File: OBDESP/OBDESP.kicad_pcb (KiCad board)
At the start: 2 copper layers, 56.8 x 26 mm, 38 parts, among them J1 USB_A, J2 RST, J3 BOOT, J4 UART, Q1 BC848CLT1G, U1 NCP1117-3.3_DPAK, U2 ESP32-WROOM-32, U3 NRF24L01_SMD

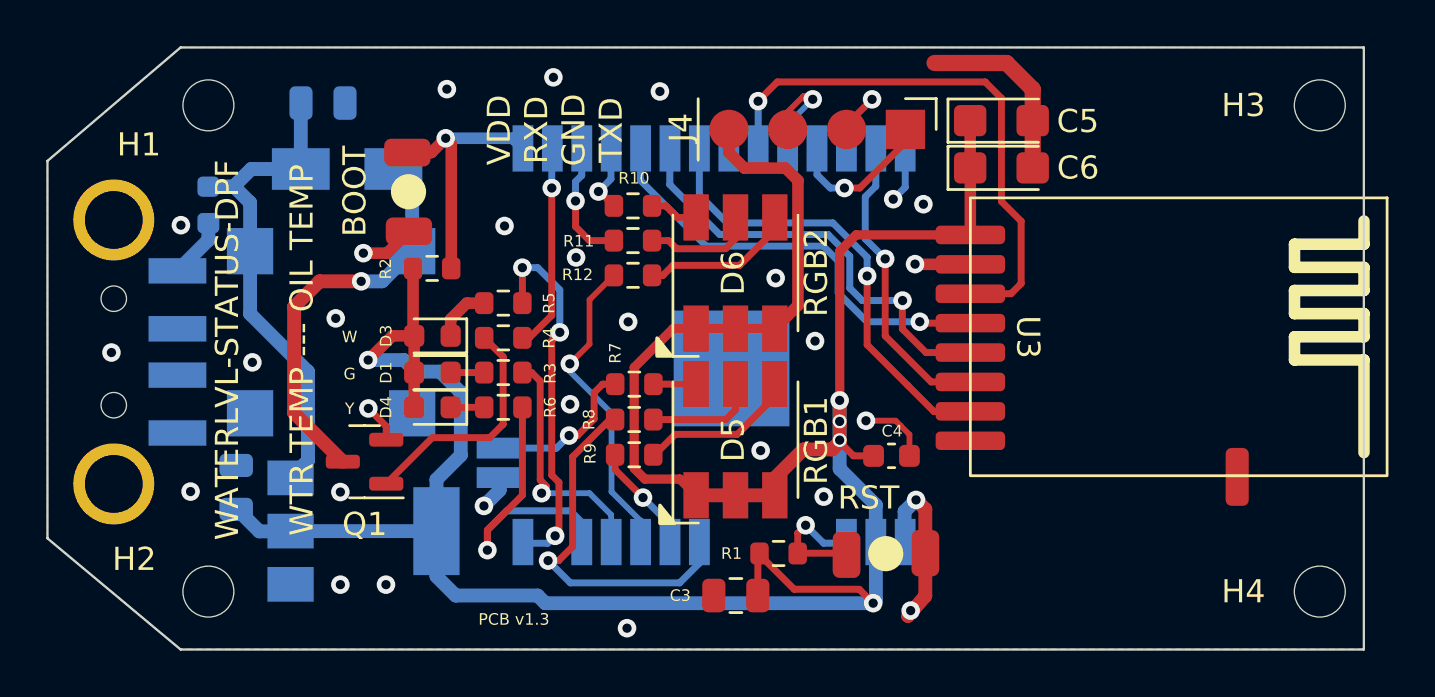
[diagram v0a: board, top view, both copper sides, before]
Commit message: Updated ODBESP32 PCB with LED separation larger.
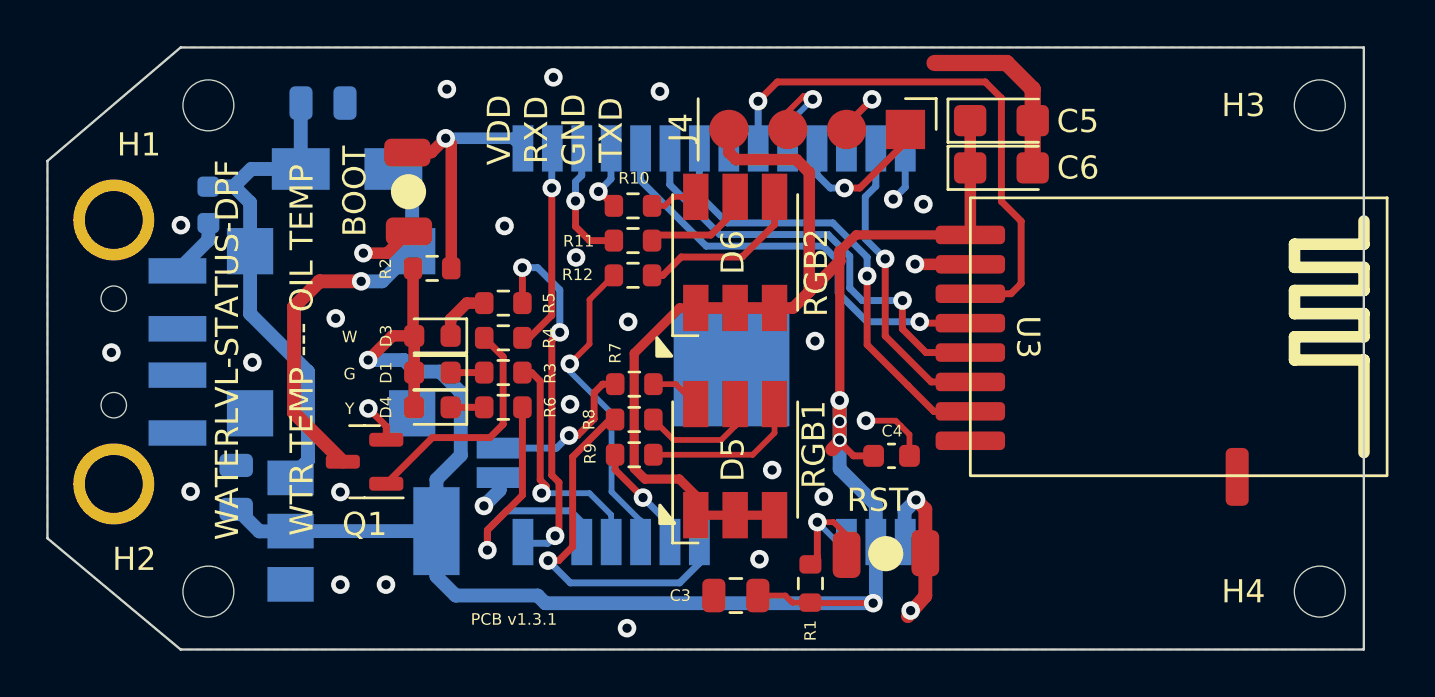
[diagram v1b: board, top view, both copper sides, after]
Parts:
- moved R1 1.89 mm to (69.7, 36.5), turned to 90 degrees
- moved D6 0.89 mm to (66.5, 22.1)
- moved D5 0.86 mm to (66.5, 31.1)
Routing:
- net /3.3V: track 120.9 -> 118.9 mm
- net Net-(D6-Pad4): track 6.66 -> 7.40 mm
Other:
- board text added: "PCB v1.3.1"
- board text removed: "PCB v1.3"

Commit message: Updated both PCBs with TEMT6000 and XKC enabler
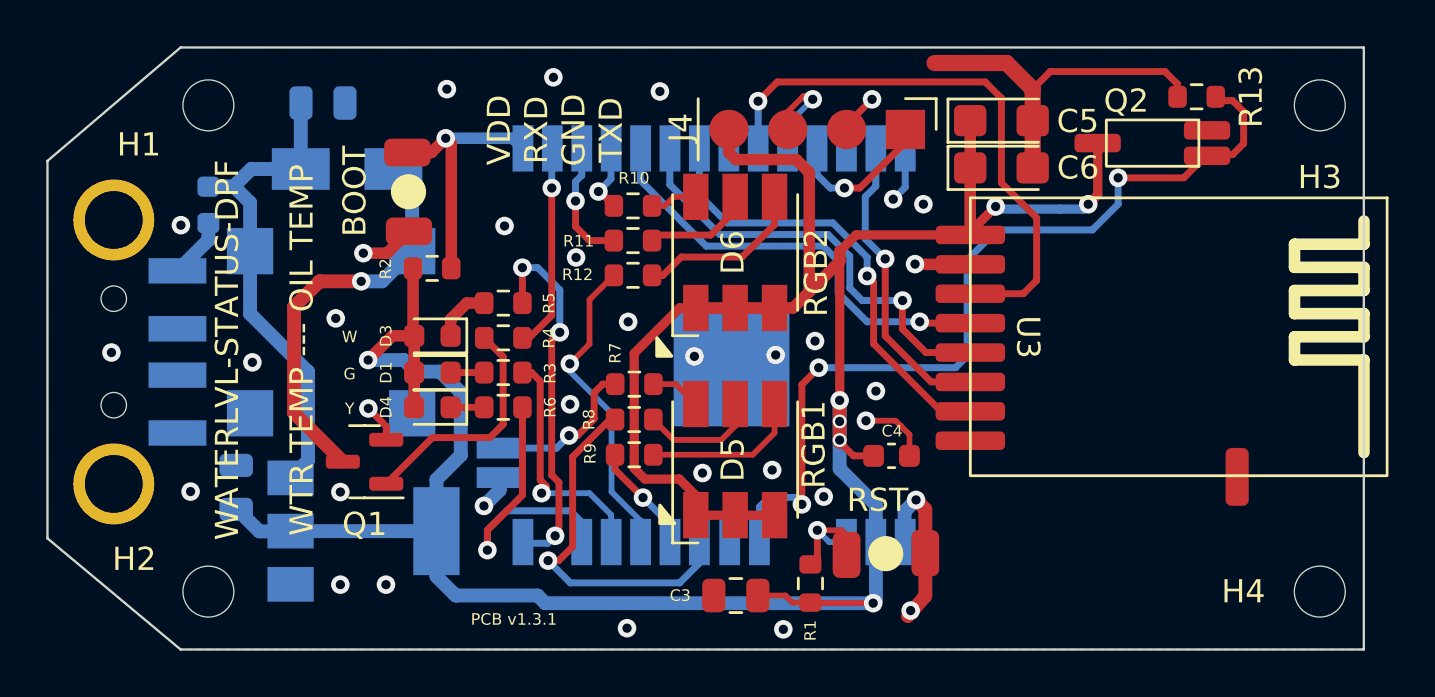
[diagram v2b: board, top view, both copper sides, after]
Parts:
- added Q2: Q_Photo_NPN_CBE, mykicad_6:TEMT6000, F.Cu at (84.5, 17.4)
- added R13: 10k, Resistor_SMD:R_0603_1608Metric, F.Cu at (86.4, 15.4)
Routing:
- net /ADC_IN: track 0.00 -> 38.2 mm, vias 0 -> 3
- net /3.3V: track 118.9 -> 127.1 mm, vias 5 -> 7
- net GND: track 31.2 -> 38.5 mm, vias 30 -> 34
- net /NRF_CE: track 23.9 -> 24.8 mm
- net Net-(J2-Pad2): track 5.90 -> 5.26 mm

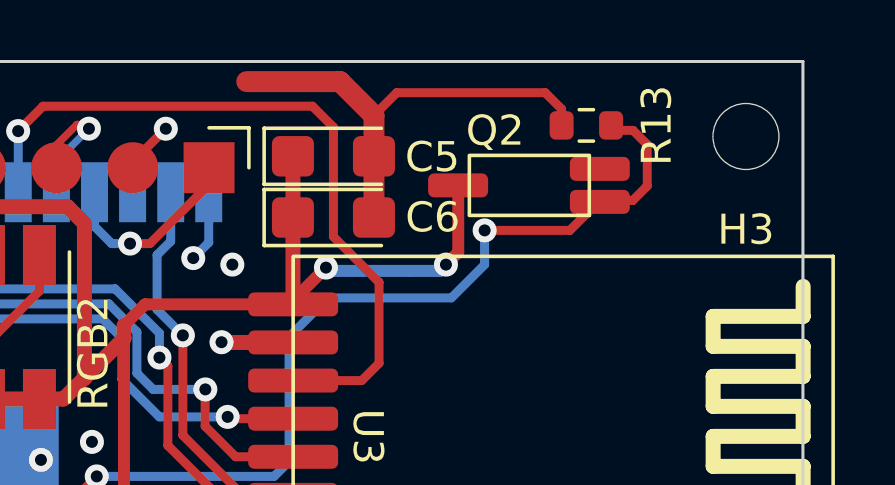
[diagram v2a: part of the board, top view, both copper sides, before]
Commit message: ESP32-added ADC functions untested! PCB update
added capacitor for PCB design for ADC reading the TEMT6000 sensor
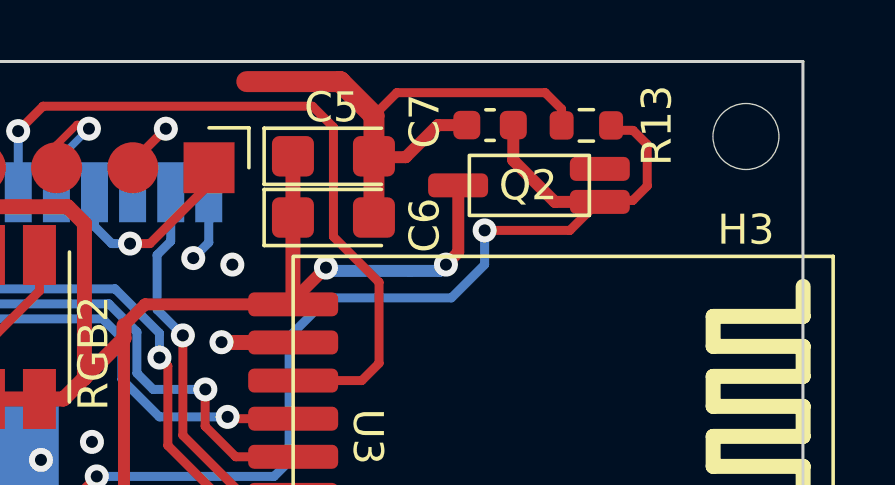
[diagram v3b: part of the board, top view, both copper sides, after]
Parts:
- added C7: 100nF, Capacitor_SMD:C_0603_1608Metric, F.Cu at (83.2, 15.4)
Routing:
- net /ADC_IN: track 38.2 -> 42.8 mm
- net GND: track 38.5 -> 42.1 mm
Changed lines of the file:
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@@
+    )
+  )
+  (footprint "Capacitor_SMD:C_0603_1608Metric" (layer "F.Cu")
+    (at 83.17 15.42)
+    (descr "Capacitor SMD 0603 (1608 Metric), square (rectangular) end terminal, IPC_7351 nominal, (Body size source: IPC-SM-782 page 76, https://www.pcb-3d.com/wordpress/wp-content/uploads/ipc-sm-782a_amendment_1_and_2.pdf), generated with kicad-footprint-generator")
+    (tags "capacitor")
+    (property "LOMEX" "82-13-28")
+    (property "Sheetfile" "OBDESP.kicad_sch")
+    (property "Sheetname" "")
+    (attr smd)
+    (fp_text reference "C7" (at -2.18 -0.13 90) (layer "F.SilkS")
+      (effects (font (size 1 1) (thickness 0.15)))
+    )
+    (fp_text value "100nF" (at 0 1.43) (layer "F.Fab")
+      (effects (font (size 1 1) (thickness 0.15)))
+    )
+    (fp_text user "${REFERENCE}" (at 0 0) (layer "F.Fab")
+      (effects (font (size 0.4 0.4) (thickness 0.06)))
+    )
+    (fp_line (start -0.14058 -0.51) (end 0.14058 -0.51) (layer "F.SilkS") (width 0.12))
+    (fp_line (start -0.14058 0.51) (end 0.14058 0.51) (layer "F.SilkS") (width 0.12))
+    (fp_line (start -1.48 0.73) (end -1.48 -0.73) (layer "F.CrtYd") (width 0.05))
+    (fp_line (start 1.48 -0.73) (end 1.48 0.73) (layer "F.CrtYd") (width 0.05))
+    (fp_line (start -1.48 -0.73) (end 1.48 -0.73) (layer "F.CrtYd") (width 0.05))
+    (fp_line (start 1.48 0.73) (end -1.48 0.73) (layer "F.CrtYd") (width 0.05))
+    (fp_line (start 0.8 0.4) (end -0.8 0.4) (layer "F.Fab") (width 0.1))
+    (fp_line (start 0.8 -0.4) (end 0.8 0.4) (layer "F.Fab") (width 0.1))
+    (fp_line (start -0.8 -0.4) (end 0.8 -0.4) (layer "F.Fab") (width 0.1))
+    (fp_line (start -0.8 0.4) (end -0.8 -0.4) (layer "F.Fab") (width 0.1))
+    (pad "1" smd roundrect (at -0.775 0) (size 0.9 0.95) (layers "F.Cu" "F.Paste" "F.Mask") (roundrect_rratio 0.25)
+      (net 1 "GND") (pintype "passive"))
+    (pad "2" smd roundrect (at 0.775 0) (size 0.9 0.95) (layers "F.Cu" "F.Paste" "F.Mask") (roundrect_rratio 0.25)
+      (net 42 "/ADC_IN") (pintype "passive"))
+    (model "${KICAD6_3DMODEL_DIR}/Capacitor_SMD.3dshapes/C_0603_1608Metric.wrl"
+      (offset (xyz 0 0 0))
+      (scale (xyz 1 1 1))
+      (rotate (xyz 0 0 0))
     )
   )
@@
     (property "Sheetname" "")
     (attr smd)
-    (fp_text reference "C5" (at 3.3 0.03) (layer "F.SilkS")
+    (fp_text reference "C5" (at -0.06 -1.63) (layer "F.SilkS")
       (effects (font (size 1 1) (thickness 0.15)))
     )
@@
     (property "Sheetname" "")
     (attr smd)
-    (fp_text reference "C6" (at 3.31 0) (layer "F.SilkS")
+    (fp_text reference "C6" (at 3.04 0.26 90) (layer "F.SilkS")
       (effects (font (size 1 1) (thickness 0.15)))
     )
@@
     (property "Sheetfile" "OBDESP.kicad_sch")
     (property "Sheetname" "")
-    (attr smd)
-    (fp_text reference "Q2" (at 1.14 1.82 unlocked) (layer "F.SilkS")
+    (property "mouser" "78-TEMT6000")
+    (attr smd)
+    (fp_text reference "Q2" (at 0.04 0 unlocked) (layer "F.SilkS")
       (effects (font (size 1 1) (thickness 0.15)))
     )
@@
   (segment (start 73.9778 30.0178) (end 73.6 29.64) (width 0.25) (layer "F.Cu") (net 1))
   (segment (start 50.3936 22.183502) (end 51.419876 22.183502) (width 0.5) (layer "F.Cu") (net 1))
+  (segment (start 79.33 16.49) (end 79.3 16.46) (width 0.4) (layer "F.Cu") (net 1))
   (segment (start 50.61 28.89) (end 51.3819 29.6619) (width 0.3) (layer "F.Cu") (net 1))
   (segment (start 85.555 14.885) (end 85.01 14.34) (width 0.3) (layer "F.Cu") (net 1))
   (segment (start 71.262489 16.640889) (end 72.362489 15.540889) (width 0.3) (layer "F.Cu") (net 1))
+  (segment (start 81.43 15.42) (end 80.36 16.49) (width 0.4) (layer "F.Cu") (net 1))
   (segment (start 79.3 15.1) (end 78.17 13.97) (width 0.7) (layer "F.Cu") (net 1))
   (segment (start 74.228 22.666) (end 74.2188 22.6568) (width 0.5) (layer "F.Cu") (net 1))
@@
   (segment (start 76.6068 22.666) (end 74.228 22.666) (width 0.5) (layer "F.Cu") (net 1))
   (segment (start 51.3819 29.6619) (end 51.3819 30.2412) (width 0.3) (layer "F.Cu") (net 1))
+  (segment (start 80.36 16.49) (end 79.33 16.49) (width 0.4) (layer "F.Cu") (net 1))
   (segment (start 79.3 18.5) (end 79.3 16.45) (width 0.7) (layer "F.Cu") (net 1))
   (segment (start 74.662489 35.140889) (end 74.662489 33.240889) (width 0.6) (layer "F.Cu") (net 1))
@@
   (segment (start 73.9778 30.9372) (end 73.9778 30.0178) (width 0.25) (layer "F.Cu") (net 1))
   (segment (start 85.01 14.34) (end 80.06 14.34) (width 0.3) (layer "F.Cu") (net 1))
+  (segment (start 82.395 15.42) (end 81.43 15.42) (width 0.4) (layer "F.Cu") (net 1))
   (segment (start 71.262489 16.840889) (end 71.262489 16.640889) (width 0.3) (layer "F.Cu") (net 1))
   (segment (start 51.419876 22.183502) (end 52.362489 21.240889) (width 0.5) (layer "F.Cu") (net 1))
@@
   (segment (start 55.75 35.01) (end 55.75 34.14) (width 0.3) (layer "B.Cu") (net 40))
   (segment (start 87.93 17.93) (end 86.83 17.93) (width 0.3) (layer "F.Cu") (net 42))
+  (segment (start 83.945 16.595) (end 83.945 15.42) (width 0.4) (layer "F.Cu") (net 42))
+  (segment (start 85.33 17.98) (end 83.945 16.595) (width 0.4) (layer "F.Cu") (net 42))
   (segment (start 88.41 17.45) (end 87.93 17.93) (width 0.3) (layer "F.Cu") (net 42))
   (segment (start 82.99 18.93) (end 85.83 18.93) (width 0.3) (layer "F.Cu") (net 42))
@@
   (segment (start 87.08 15.595) (end 87.935 15.595) (width 0.3) (layer "F.Cu") (net 42))
   (segment (start 85.83 18.93) (end 86.83 17.93) (width 0.3) (layer "F.Cu") (net 42))
+  (segment (start 86.83 17.98) (end 85.33 17.98) (width 0.4) (layer "F.Cu") (net 42))
   (segment (start 70.06 27.13) (end 69.33226 27.85774) (width 0.3) (layer "F.Cu") (net 42))
   (via (at 69.33226 33.032034) (size 0.8) (drill 0.4) (layers "F.Cu" "B.Cu") (net 42))

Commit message: latest versions
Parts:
- removed C7: 100nF, Capacitor_SMD:C_0603_1608Metric
- removed Q2: Q_Photo_NPN_CBE, mykicad_6:TEMT6000
- removed R13: 10k, Resistor_SMD:R_0603_1608Metric
- D3: value WHITE_LED -> YELLOW_LED
- D4: value YELLOW_OIL_LED -> WHITE_LED
- R5: value 100 -> 220
- R6: value 220 -> 100
- moved D4 30.9 mm to (83.2, 36.8), turned to -90 degrees
- moved R6 29.6 mm to (85.0, 36.8), turned to 90 degrees
- moved D3 4.52 mm to (55.6, 21.8), turned to 90 degrees
- moved J3 2.32 mm to (50.0, 19.5)
- moved R2 1.26 mm to (52.5, 21.9), turned to 90 degrees
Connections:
- net /STATUS_LED renamed /STATUS1_LED
- R5 pad 1: /WATER_LED -> /COOLANTSTATUS_LED
- U2 pad 12: /DPF_LED -> /COOLANTSTATUS_LED
- U2 pad 14: /WATER_LED -> /DPF_LED
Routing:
- net /ADC_IN: track 42.8 -> 0.00 mm, vias 3 -> 0
- net /DPF_LED: track 13.1 -> 34.9 mm
- net /WATER_LED: track 16.0 -> 0.00 mm, vias 3 -> 0
- net /COOLANTSTATUS_LED: track 0.00 -> 15.9 mm, vias 0 -> 3
- net GND: track 42.1 -> 28.6 mm, vias 34 -> 35
- net /3.3V: track 127.1 -> 131.7 mm, vias 7 -> 6
- net Net-(R5-Pad2): track 2.46 -> 1.74 mm
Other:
- board text added: "DPF"
- board text added: "PCB v1.4"
- board text removed: "G"
- board text removed: "PCB v1.3.1"
- board text removed: "W"
- board text removed: "Y"
